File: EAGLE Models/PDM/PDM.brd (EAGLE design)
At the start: 160 x 100 mm, 15 parts

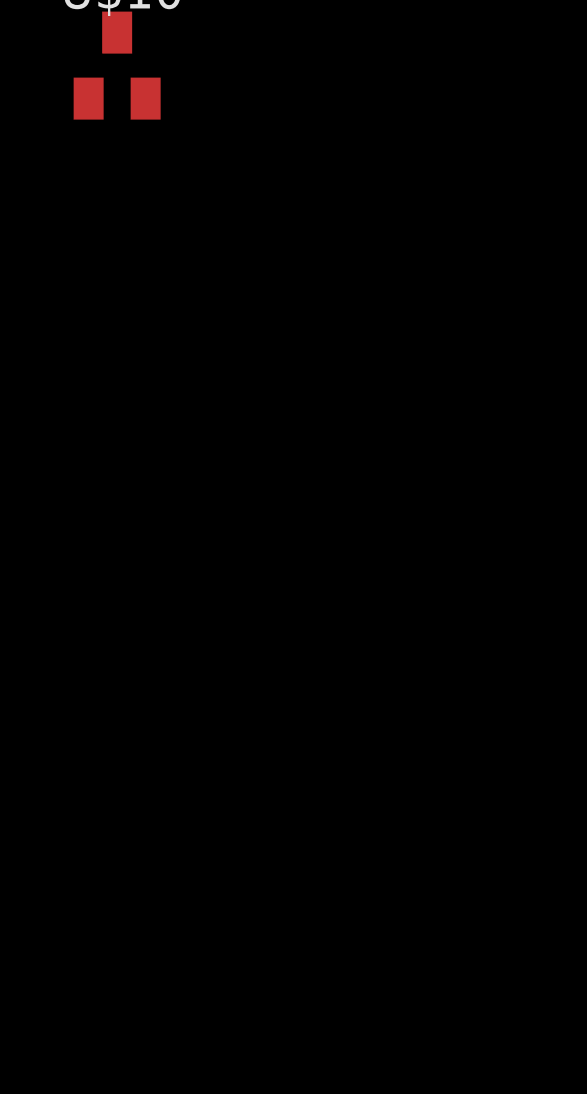
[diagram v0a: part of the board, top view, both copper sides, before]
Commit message: Finished schematic for PDM
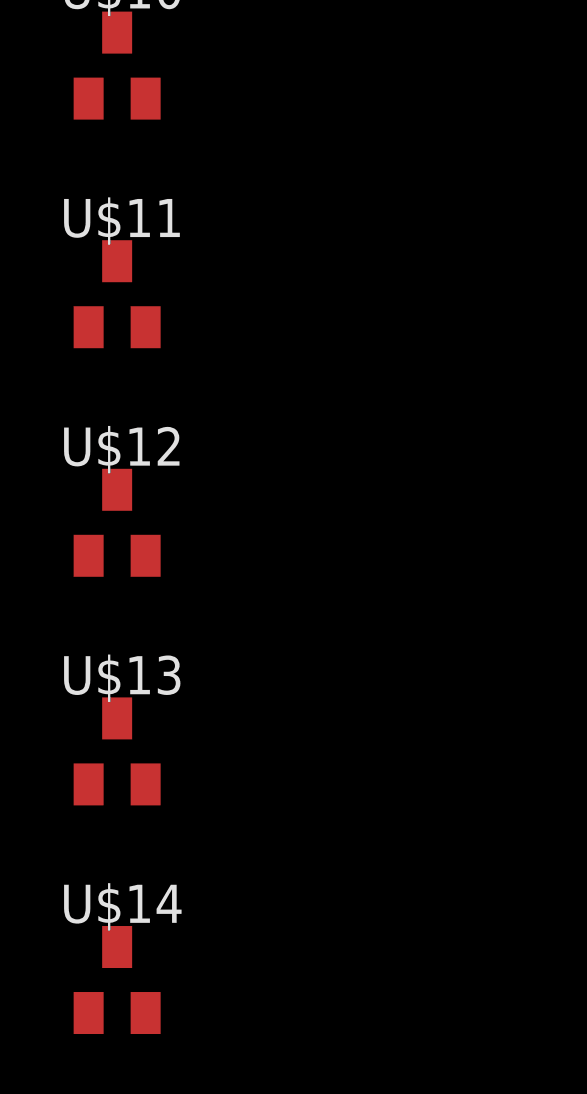
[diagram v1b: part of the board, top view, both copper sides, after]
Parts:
- added U$11, U$12, U$13, U$14: MMBD4448H-7-F, diodes-inc:SOT23-3
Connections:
- removed net KILL_SWT_IN: U$10.3, U$6.COIL1
- removed net N$1: U$6.NO
- new net MAIN_RELAY_IN: U$10.3, U$14.3, U$6.COIL1
- net 12V: now also U$11.3, U$12.3, U$13.3, U$6.NO
- net A23: now also U$13.1
- net A24: now also U$11.1, U$12.1
- net GND: now also U$14.1
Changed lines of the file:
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@@
 <element name="U$9" library="molex" package="15-97-8043" value="15-97-8043" x="-60.96" y="66.04"/>
 <element name="U$10" library="diodes-inc" package="SOT23-3" value="MMBD4448H-7-F" x="-69.85" y="-12.7"/>
+<element name="U$11" library="diodes-inc" package="SOT23-3" value="MMBD4448H-7-F" x="-69.85" y="-20.32"/>
+<element name="U$12" library="diodes-inc" package="SOT23-3" value="MMBD4448H-7-F" x="-69.85" y="-27.94"/>
+<element name="U$13" library="diodes-inc" package="SOT23-3" value="MMBD4448H-7-F" x="-69.85" y="-35.56"/>
+<element name="U$14" library="diodes-inc" package="SOT23-3" value="MMBD4448H-7-F" x="-69.85" y="-43.18"/>
 </elements>
 <signals>
@@
 <contactref element="U$3" pad="COIL1"/>
 <contactref element="U$1" pad="4"/>
+<contactref element="U$13" pad="1"/>
+<wire x1="-46.101" y1="4.8641" x2="-70.8" y2="-36.66" width="0" layer="19" extent="1-1"/>
 <wire x1="-22.987" y1="24.5618" x2="-46.101" y2="4.8641" width="0" layer="19" extent="1-1"/>
 </signal>
@@
 <contactref element="U$5" pad="COIL1"/>
 <contactref element="U$1" pad="3"/>
-<wire x1="-37.719" y1="10.3759" x2="-48.387" y2="24.5618" width="0" layer="19" extent="1-1"/>
+<contactref element="U$11" pad="1"/>
+<contactref element="U$12" pad="1"/>
+<wire x1="-70.8" y1="-21.42" x2="-70.8" y2="-29.04" width="0" layer="19" extent="1-1"/>
+<wire x1="-37.719" y1="10.3759" x2="-70.8" y2="-21.42" width="0" layer="19" extent="1-1"/>
+<wire x1="-48.387" y1="24.5618" x2="-37.719" y2="10.3759" width="0" layer="19" extent="1-1"/>
 <wire x1="-22.987" y1="35.9918" x2="-48.387" y2="24.5618" width="0" layer="19" extent="1-1"/>
 </signal>
@@
 <contactref element="U$8" pad="5"/>
 <contactref element="U$7" pad="COIL2"/>
+<contactref element="U$14" pad="1"/>
+<wire x1="-24.9555" y1="4.8641" x2="-70.8" y2="-44.28" width="0" layer="19" extent="1-1"/>
+<wire x1="-20.7645" y1="4.8641" x2="-24.9555" y2="4.8641" width="0" layer="19" extent="1-1"/>
+<wire x1="-16.5735" y1="4.8641" x2="-20.7645" y2="4.8641" width="0" layer="19" extent="1-1"/>
+<wire x1="-22.987" y1="42.5704" x2="-24.9555" y2="4.8641" width="0" layer="19" extent="1-1"/>
+<wire x1="-45.7835" y1="68.7959" x2="-22.987" y2="42.5704" width="0" layer="19" extent="1-1"/>
 <wire x1="-49.9745" y1="68.7959" x2="-45.7835" y2="68.7959" width="0" layer="19" extent="1-1"/>
 <wire x1="-54.1655" y1="68.7959" x2="-49.9745" y2="68.7959" width="0" layer="19" extent="1-1"/>
-<wire x1="-22.987" y1="42.5704" x2="-45.7835" y2="68.7959" width="0" layer="19" extent="1-1"/>
-<wire x1="-24.9555" y1="4.8641" x2="-22.987" y2="42.5704" width="0" layer="19" extent="1-1"/>
-<wire x1="-20.7645" y1="4.8641" x2="-24.9555" y2="4.8641" width="0" layer="19" extent="1-1"/>
-<wire x1="-16.5735" y1="4.8641" x2="-20.7645" y2="4.8641" width="0" layer="19" extent="1-1"/>
 </signal>
 <signal name="BAT_+12">
@@
 <wire x1="-48.387" y1="31.1404" x2="-22.987" y2="47.4218" width="0" layer="19" extent="1-1"/>
 </signal>
-<signal name="KILL_SWT_IN">
+<signal name="MAIN_RELAY_IN">
 <contactref element="U$10" pad="3"/>
 <contactref element="U$6" pad="COIL1"/>
+<contactref element="U$14" pad="3"/>
+<wire x1="-69.85" y1="-11.6" x2="-69.85" y2="-42.08" width="0" layer="19" extent="1-1"/>
 <wire x1="-48.387" y1="35.9918" x2="-69.85" y2="-11.6" width="0" layer="19" extent="1-1"/>
-</signal>
-<signal name="N$1">
-<contactref element="U$6" pad="NO"/>
 </signal>
 <signal name="12V">
@@
 <contactref element="U$4" pad="COIL2"/>
 <contactref element="U$3" pad="COIL2"/>
+<contactref element="U$11" pad="3"/>
+<contactref element="U$12" pad="3"/>
+<contactref element="U$6" pad="NO"/>
+<contactref element="U$13" pad="3"/>
+<wire x1="-69.85" y1="-26.84" x2="-69.85" y2="-34.46" width="0" layer="19" extent="1-1"/>
+<wire x1="-69.85" y1="-19.22" x2="-69.85" y2="-26.84" width="0" layer="19" extent="1-1"/>
+<wire x1="-48.387" y1="19.7104" x2="-69.85" y2="-19.22" width="0" layer="19" extent="1-1"/>
+<wire x1="-56.8452" y1="34.29" x2="-48.387" y2="19.7104" width="0" layer="19" extent="1-1"/>
+<wire x1="-59.563" y1="54.1782" x2="-56.8452" y2="34.29" width="0" layer="19" extent="1-1"/>
+<wire x1="-59.563" y1="57.5818" x2="-59.563" y2="54.1782" width="0" layer="19" extent="1-1"/>
+<wire x1="-43.053" y1="57.5818" x2="-59.563" y2="57.5818" width="0" layer="19" extent="1-1"/>
+<wire x1="-43.053" y1="54.1782" x2="-43.053" y2="57.5818" width="0" layer="19" extent="1-1"/>
+<wire x1="-43.053" y1="64.3382" x2="-43.053" y2="57.5818" width="0" layer="19" extent="1-1"/>
+<wire x1="-43.053" y1="67.7418" x2="-43.053" y2="64.3382" width="0" layer="19" extent="1-1"/>
+<wire x1="-26.543" y1="67.7418" x2="-43.053" y2="67.7418" width="0" layer="19" extent="1-1"/>
 <wire x1="-26.543" y1="64.3382" x2="-26.543" y2="67.7418" width="0" layer="19" extent="1-1"/>
 <wire x1="-26.543" y1="57.5818" x2="-26.543" y2="64.3382" width="0" layer="19" extent="1-1"/>
 <wire x1="-26.543" y1="54.1782" x2="-26.543" y2="57.5818" width="0" layer="19" extent="1-1"/>
-<wire x1="-43.053" y1="67.7418" x2="-26.543" y2="67.7418" width="0" layer="19" extent="1-1"/>
-<wire x1="-43.053" y1="64.3382" x2="-43.053" y2="67.7418" width="0" layer="19" extent="1-1"/>
-<wire x1="-43.053" y1="57.5818" x2="-43.053" y2="64.3382" width="0" layer="19" extent="1-1"/>
-<wire x1="-43.053" y1="54.1782" x2="-43.053" y2="57.5818" width="0" layer="19" extent="1-1"/>
-<wire x1="-59.563" y1="54.1782" x2="-43.053" y2="54.1782" width="0" layer="19" extent="1-1"/>
-<wire x1="-59.563" y1="57.5818" x2="-59.563" y2="54.1782" width="0" layer="19" extent="1-1"/>
 <wire x1="-22.987" y1="31.1404" x2="-26.543" y2="54.1782" width="0" layer="19" extent="1-1"/>
 <wire x1="-22.987" y1="19.7104" x2="-22.987" y2="31.1404" width="0" layer="19" extent="1-1"/>
-<wire x1="-48.387" y1="19.7104" x2="-22.987" y2="19.7104" width="0" layer="19" extent="1-1"/>
 </signal>
 </signals>

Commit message: Updated Connectors, Changed Schematic
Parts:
- removed U$14: MMBD4448H-7-F, diodes-inc:SOT23-3
- removed U$6: ACTP112ACTP112, panasonic:ACTP112
- added F1: 3568, Keystone:3568
- added U$15: VCF4-1000, relay:VCF4-1000
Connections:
- new net BAT_+12_FUSED: F1.3, F1.4, U$1.1
- net 12V: now also U$15.NO; no longer U$6.NO
- net BAT_+12: now also F1.1, F1.2, U$15.COM; no longer U$1.1, U$6.COM
- net CHARGE_CUT_IN: now also U$15.COIL2; no longer U$6.COIL2
- net GND: no longer U$14.1
- net MAIN_RELAY_IN: now also U$15.COIL1; no longer U$14.3, U$6.COIL1
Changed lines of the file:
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@@
 <element name="U$4" library="panasonic" package="ACTP112" value="ACTP112ACTP112" x="-53.34" y="19.05"/>
 <element name="U$5" library="panasonic" package="ACTP112" value="ACTP112ACTP112" x="-27.94" y="30.48"/>
-<element name="U$6" library="panasonic" package="ACTP112" value="ACTP112ACTP112" x="-53.34" y="30.48"/>
 <element name="U$7" library="panasonic" package="ACTP112" value="ACTP112ACTP112" x="-27.94" y="41.91"/>
 <element name="U$8" library="molex" package="15-97-7084" value="15-97-7084" x="-52.07" y="66.04"/>
@@
 <element name="U$12" library="diodes-inc" package="SOT23-3" value="MMBD4448H-7-F" x="-69.85" y="-27.94"/>
 <element name="U$13" library="diodes-inc" package="SOT23-3" value="MMBD4448H-7-F" x="-69.85" y="-35.56"/>
-<element name="U$14" library="diodes-inc" package="SOT23-3" value="MMBD4448H-7-F" x="-69.85" y="-43.18"/>
+<element name="F1" library="Keystone" package="3568" value="3568" x="-55.88" y="-60.96"/>
+<element name="U$15" library="relay" package="VCF4-1000" value="VCF4-1000" x="-46.99" y="-100.33"/>
 </elements>
 <signals>
@@
 <contactref element="U$8" pad="5"/>
 <contactref element="U$7" pad="COIL2"/>
-<contactref element="U$14" pad="1"/>
-<wire x1="-24.9555" y1="4.8641" x2="-70.8" y2="-44.28" width="0" layer="19" extent="1-1"/>
+<wire x1="-49.9745" y1="68.7959" x2="-45.7835" y2="68.7959" width="0" layer="19" extent="1-1"/>
+<wire x1="-54.1655" y1="68.7959" x2="-49.9745" y2="68.7959" width="0" layer="19" extent="1-1"/>
+<wire x1="-22.987" y1="42.5704" x2="-45.7835" y2="68.7959" width="0" layer="19" extent="1-1"/>
+<wire x1="-24.9555" y1="4.8641" x2="-22.987" y2="42.5704" width="0" layer="19" extent="1-1"/>
 <wire x1="-20.7645" y1="4.8641" x2="-24.9555" y2="4.8641" width="0" layer="19" extent="1-1"/>
 <wire x1="-16.5735" y1="4.8641" x2="-20.7645" y2="4.8641" width="0" layer="19" extent="1-1"/>
-<wire x1="-22.987" y1="42.5704" x2="-24.9555" y2="4.8641" width="0" layer="19" extent="1-1"/>
-<wire x1="-45.7835" y1="68.7959" x2="-22.987" y2="42.5704" width="0" layer="19" extent="1-1"/>
-<wire x1="-49.9745" y1="68.7959" x2="-45.7835" y2="68.7959" width="0" layer="19" extent="1-1"/>
-<wire x1="-54.1655" y1="68.7959" x2="-49.9745" y2="68.7959" width="0" layer="19" extent="1-1"/>
 </signal>
 <signal name="BAT_+12">
 <contactref element="U$9" pad="2"/>
 <contactref element="U$9" pad="1"/>
-<contactref element="U$1" pad="1"/>
-<contactref element="U$6" pad="COM"/>
 <contactref element="U$7" pad="NO"/>
-<wire x1="-62.8396" y1="31.1404" x2="-46.101" y2="10.3759" width="0" layer="19" extent="1-1"/>
-<wire x1="-63.06058125" y1="63.2841" x2="-62.8396" y2="31.1404" width="0" layer="19" extent="1-1"/>
-<wire x1="-58.85941875" y1="63.2841" x2="-63.06058125" y2="63.2841" width="0" layer="19" extent="1-1"/>
-<wire x1="-31.4452" y1="45.72" x2="-58.85941875" y2="63.2841" width="0" layer="19" extent="1-1"/>
+<contactref element="F1" pad="1"/>
+<contactref element="F1" pad="2"/>
+<contactref element="U$15" pad="COM"/>
+<wire x1="-60.833" y1="-62.6618" x2="-37.4904" y2="-100.33" width="0" layer="19" extent="1-1"/>
+<wire x1="-60.833" y1="-59.2582" x2="-60.833" y2="-62.6618" width="0" layer="19" extent="1-1"/>
+<wire x1="-31.4452" y1="45.72" x2="-60.833" y2="-59.2582" width="0" layer="19" extent="1-1"/>
+<wire x1="-58.85941875" y1="63.2841" x2="-31.4452" y2="45.72" width="0" layer="19" extent="1-1"/>
+<wire x1="-63.06058125" y1="63.2841" x2="-58.85941875" y2="63.2841" width="0" layer="19" extent="1-1"/>
 </signal>
 <signal name="BAT_GND">
@@
 </signal>
 <signal name="CHARGE_CUT_IN">
-<contactref element="U$6" pad="COIL2"/>
 <contactref element="U$7" pad="COIL1"/>
-<wire x1="-48.387" y1="31.1404" x2="-22.987" y2="47.4218" width="0" layer="19" extent="1-1"/>
+<contactref element="U$15" pad="COIL2"/>
+<wire x1="-22.987" y1="47.4218" x2="-46.99" y2="-91.8845" width="0" layer="19" extent="1-1"/>
 </signal>
 <signal name="MAIN_RELAY_IN">
 <contactref element="U$10" pad="3"/>
-<contactref element="U$6" pad="COIL1"/>
-<contactref element="U$14" pad="3"/>
-<wire x1="-69.85" y1="-11.6" x2="-69.85" y2="-42.08" width="0" layer="19" extent="1-1"/>
-<wire x1="-48.387" y1="35.9918" x2="-69.85" y2="-11.6" width="0" layer="19" extent="1-1"/>
+<contactref element="U$15" pad="COIL1"/>
+<wire x1="-69.85" y1="-11.6" x2="-46.99" y2="-108.7755" width="0" layer="19" extent="1-1"/>
 </signal>
 <signal name="12V">
@@
 <contactref element="U$11" pad="3"/>
 <contactref element="U$12" pad="3"/>
-<contactref element="U$6" pad="NO"/>
 <contactref element="U$13" pad="3"/>
+<contactref element="U$15" pad="NO"/>
+<wire x1="-69.85" y1="-34.46" x2="-55.3974" y2="-100.33" width="0" layer="19" extent="1-1"/>
 <wire x1="-69.85" y1="-26.84" x2="-69.85" y2="-34.46" width="0" layer="19" extent="1-1"/>
 <wire x1="-69.85" y1="-19.22" x2="-69.85" y2="-26.84" width="0" layer="19" extent="1-1"/>
 <wire x1="-48.387" y1="19.7104" x2="-69.85" y2="-19.22" width="0" layer="19" extent="1-1"/>
-<wire x1="-56.8452" y1="34.29" x2="-48.387" y2="19.7104" width="0" layer="19" extent="1-1"/>
-<wire x1="-59.563" y1="54.1782" x2="-56.8452" y2="34.29" width="0" layer="19" extent="1-1"/>
+<wire x1="-22.987" y1="19.7104" x2="-48.387" y2="19.7104" width="0" layer="19" extent="1-1"/>
+<wire x1="-22.987" y1="31.1404" x2="-22.987" y2="19.7104" width="0" layer="19" extent="1-1"/>
+<wire x1="-26.543" y1="54.1782" x2="-22.987" y2="31.1404" width="0" layer="19" extent="1-1"/>
+<wire x1="-26.543" y1="57.5818" x2="-26.543" y2="54.1782" width="0" layer="19" extent="1-1"/>
+<wire x1="-26.543" y1="64.3382" x2="-26.543" y2="57.5818" width="0" layer="19" extent="1-1"/>
+<wire x1="-26.543" y1="67.7418" x2="-26.543" y2="64.3382" width="0" layer="19" extent="1-1"/>
+<wire x1="-43.053" y1="67.7418" x2="-26.543" y2="67.7418" width="0" layer="19" extent="1-1"/>
+<wire x1="-43.053" y1="64.3382" x2="-43.053" y2="67.7418" width="0" layer="19" extent="1-1"/>
+<wire x1="-43.053" y1="57.5818" x2="-43.053" y2="64.3382" width="0" layer="19" extent="1-1"/>
+<wire x1="-43.053" y1="54.1782" x2="-43.053" y2="57.5818" width="0" layer="19" extent="1-1"/>
+<wire x1="-59.563" y1="54.1782" x2="-43.053" y2="54.1782" width="0" layer="19" extent="1-1"/>
 <wire x1="-59.563" y1="57.5818" x2="-59.563" y2="54.1782" width="0" layer="19" extent="1-1"/>
-<wire x1="-43.053" y1="57.5818" x2="-59.563" y2="57.5818" width="0" layer="19" extent="1-1"/>
-<wire x1="-43.053" y1="54.1782" x2="-43.053" y2="57.5818" width="0" layer="19" extent="1-1"/>
-<wire x1="-43.053" y1="64.3382" x2="-43.053" y2="57.5818" width="0" layer="19" extent="1-1"/>
-<wire x1="-43.053" y1="67.7418" x2="-43.053" y2="64.3382" width="0" layer="19" extent="1-1"/>
-<wire x1="-26.543" y1="67.7418" x2="-43.053" y2="67.7418" width="0" layer="19" extent="1-1"/>
-<wire x1="-26.543" y1="64.3382" x2="-26.543" y2="67.7418" width="0" layer="19" extent="1-1"/>
-<wire x1="-26.543" y1="57.5818" x2="-26.543" y2="64.3382" width="0" layer="19" extent="1-1"/>
-<wire x1="-26.543" y1="54.1782" x2="-26.543" y2="57.5818" width="0" layer="19" extent="1-1"/>
-<wire x1="-22.987" y1="31.1404" x2="-26.543" y2="54.1782" width="0" layer="19" extent="1-1"/>
-<wire x1="-22.987" y1="19.7104" x2="-22.987" y2="31.1404" width="0" layer="19" extent="1-1"/>
+</signal>
+<signal name="BAT_+12_FUSED">
+<contactref element="U$1" pad="1"/>
+<contactref element="F1" pad="3"/>
+<contactref element="F1" pad="4"/>
+<wire x1="-50.927" y1="-59.2582" x2="-50.927" y2="-62.6618" width="0" layer="19" extent="1-1"/>
+<wire x1="-46.101" y1="10.3759" x2="-50.927" y2="-59.2582" width="0" layer="19" extent="1-1"/>
 </signal>
 </signals>
